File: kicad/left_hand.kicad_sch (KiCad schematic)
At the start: 33 parts, among them SW10 Gateron_ks_27, SW11 Gateron_ks_27, SW12 Gateron_ks_27, SW13 Gateron_ks_27, SW14 Gateron_ks_27, SW15 Gateron_ks_27, SW16 Gateron_ks_27, SW17 Gateron_ks_27, SW18 Gateron_ks_27, SW19 Gateron_ks_27, SW2 SW_LED_DIODE, SW20 Gateron_ks_27, SW21 Gateron_ks_27, SW22 Gateron_ks_27, SW23 Gateron_ks_27, SW24 Gateron_ks_27, SW25 Gateron_ks_27, SW26 Gateron_ks_27, SW27 Gateron_ks_27, SW28 Gateron_ks_27, SW29 Gateron_ks_27, SW3 SW_LED_DIODE, SW30 Gateron_ks_27, SW31 Gateron_ks_27, SW32 Gateron_ks_27, SW33 Gateron_ks_27, SW4 SW_LED_DIODE, SW5 SW_LED_DIODE, SW6 Gateron_ks_27, SW7 Gateron_ks_27, SW8 Gateron_ks_27, SW9 Gateron_ks_27, U2 74HC595

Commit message: TMP: fixing RES and RST
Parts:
- SW10, SW11, SW12, SW13, SW14, SW15, SW16, SW17, SW18, SW19, SW20, SW21, SW22, SW23, SW24, SW25, SW26, SW27, SW28, SW29, SW30, SW31, SW32, SW33, SW6, SW7, SW8, SW9: symbol Keyboard:Gateron_ks_27 -> keyboard:Gateron_ks_27
- SW2, SW3, SW4, SW5: symbol Keyboard:SW_LED_DIODE -> keyboard:SW_LED_DIODE
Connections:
- net RST is gone; now on net 5V: U2.10 (~{SRCLR})

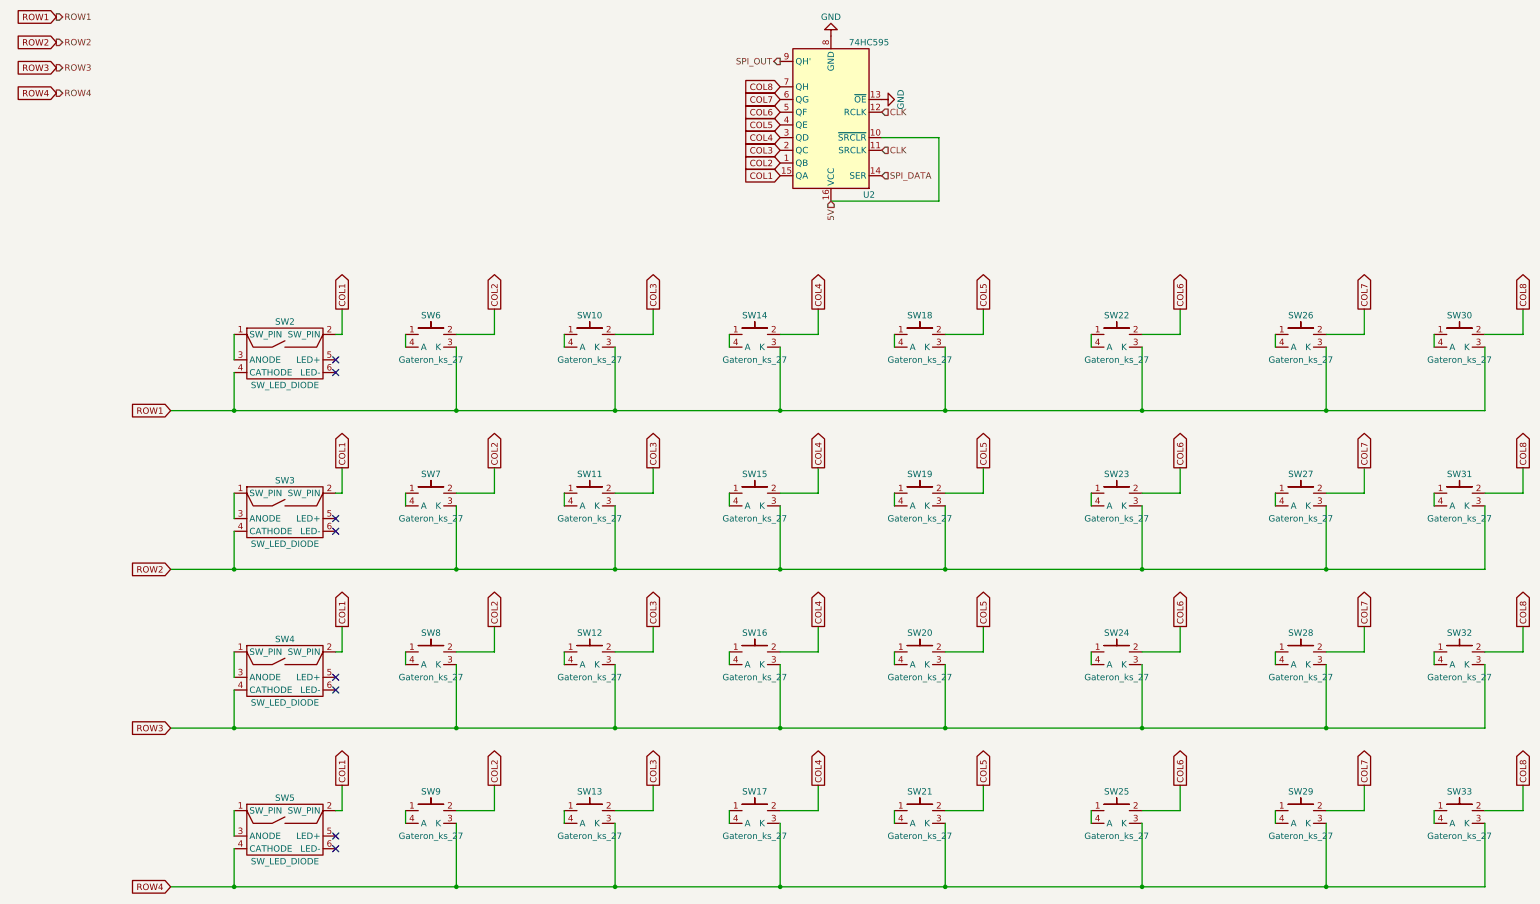
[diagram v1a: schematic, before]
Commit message: TMP: remove unused stuff
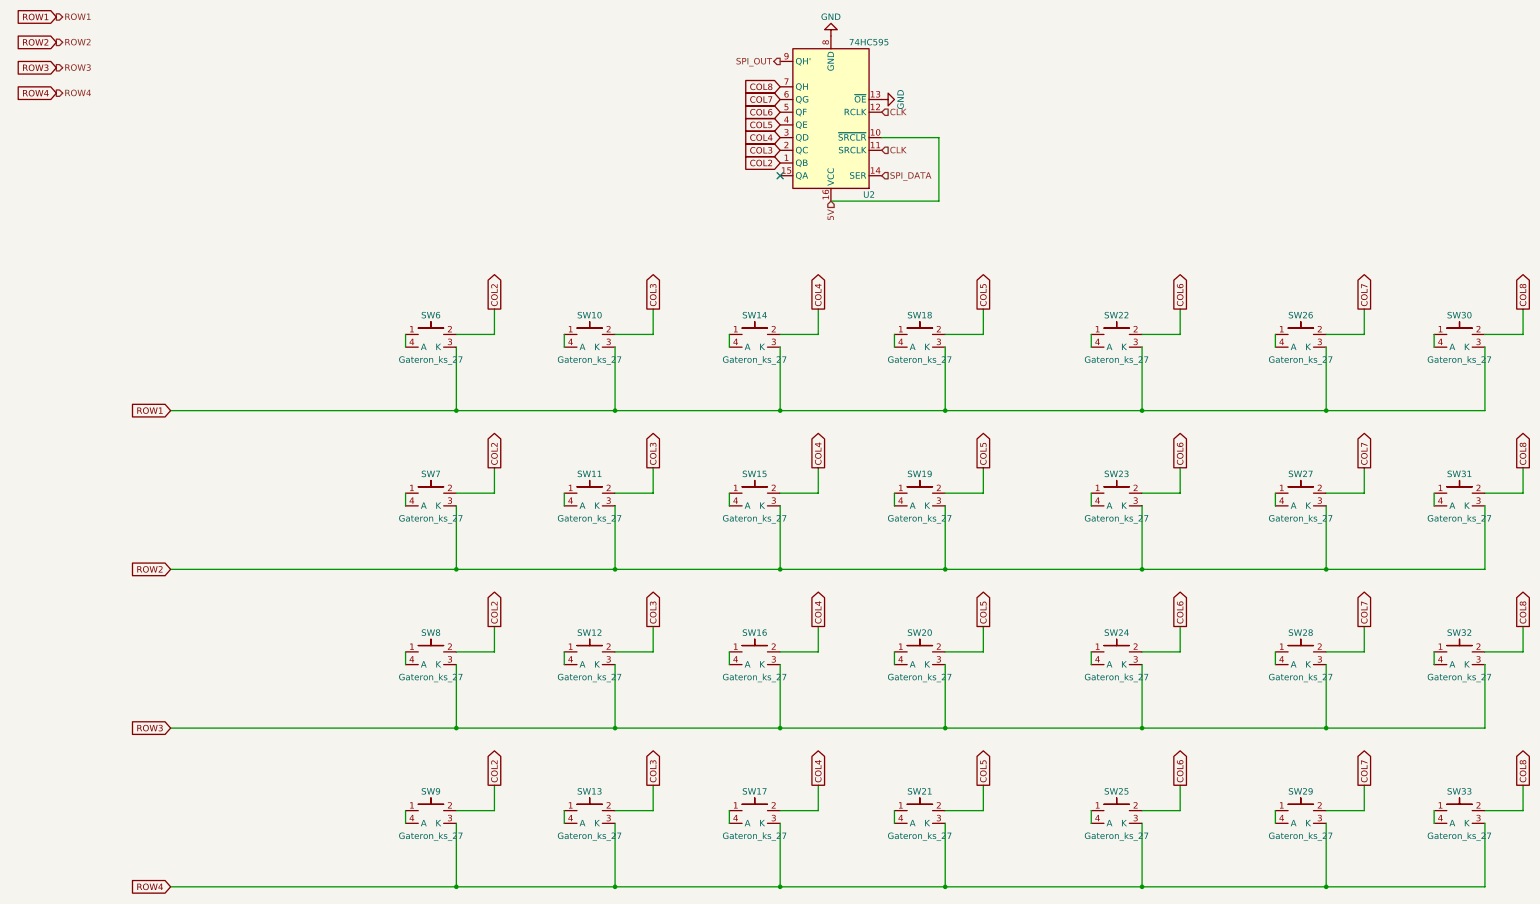
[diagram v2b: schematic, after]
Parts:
- removed SW2, SW3, SW4, SW5: SW_LED_DIODE, Keyboard:SW_LED_ext_DIODE, symbol keyboard:SW_LED_DIODE
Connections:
- net COL1: no longer names the net of U2.15 (QA)
- no-connect marks 8 -> 1
